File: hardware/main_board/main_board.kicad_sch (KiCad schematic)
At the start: 19 parts, among them IC1 E22-900M22S, IC2 INA226AIDGST, IC3 INA226AIDGST, J3 I2C External Modules, U2 ESP32-C3_SUPERMINI, U3 DS3231SN, U4 FM24CL16B

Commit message: final schema
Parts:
- removed R3: 10k, Resistor_SMD:R_0603_1608Metric, symbol Device:R_Small
- removed U2: ESP32-C3_SUPERMINI, esp32c3_super_mini:MODULE_ESP32-C3_SUPERMINI, symbol ESP32-C3_SUPERMINI:ESP32-C3_SUPERMINI
- added C1, C4: 10uF, Capacitor_SMD:C_0603_1608Metric, symbol Device:C_Small
- added C2: 100nF, Capacitor_SMD:C_0603_1608Metric, symbol Device:C_Small
- added C5, C7: DNP, Capacitor_SMD:C_0603_1608Metric, symbol Device:C_Small
- added C6: 1uF, Capacitor_SMD:C_0603_1608Metric, symbol Device:C_Small
- added J1: EXTERNAL RESET, Connector_JST:JST_EH_B2B-EH-A_1x02_P2.50mm_Vertical, symbol Connector_Generic:Conn_01x02
- added R1, R7: 0R, Resistor_SMD:R_0603_1608Metric, symbol Device:R_Small
- added R10, R12: 10k, Resistor_SMD:R_0603_1608Metric, symbol Device:R_Small
- added R13: 47k, Resistor_SMD:R_0603_1608Metric, symbol Device:R_Small
- added R4: 22R, Resistor_SMD:R_0603_1608Metric, symbol Device:R_Small
- added R8, R9: 4.7k, Resistor_SMD:R_0603_1608Metric, symbol Device:R_Small
- added SW1: RESET, Button_Switch_THT:SW_PUSH_6mm_H5mm, symbol Switch:SW_Push
- added SW2: BOOT, Button_Switch_THT:SW_PUSH_6mm_H5mm, symbol Switch:SW_Push
- added U1: ESP32-C3-WROOM-02, RF_Module:ESP32-C3-WROOM-02, symbol RF_Module:ESP32-C3-WROOM-02
- C10: renamed from C4; Comment (none) -> X7R, ±10%, 16 V
- C11: renamed from C5; Comment (none) -> X7R, ±10%, 16 V
- C3: renamed from C1; Comment (none) -> X7R, ±10%, 16 V
- C8: renamed from C2; Comment (none) -> X7R, ±10%, 16 V
- C9: renamed from C3; Comment (none) -> X7R, ±10%, 16 V
- R11: renamed from R4; Comment (none) -> RF matching element. Populate 0R initially. Value may be ch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
- R5: value 4.7k -> 22R
- R6: value 4.7k -> 470R
- renumbered J3 to J2, R1 to R2, R2 to R3, U3 to U2, U4 to U3
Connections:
- net +3V3: now also J2.2 (Pin_2), C1.1, C2.1, C4.1, R10.1, R12.2, R8.2, R9.2, U1.1 (3V3); no longer J2.1 (Pin_1), R5.2, R6.2
- net CHARGE_SOURCE_STATUS_OUT: now also R12.1, U1.5 (IO6)
- net GND: now also J2.1 (Pin_1), C1.2, C2.2, C4.2, C5.2, C6.2, C7.2, J1.2 (Pin_2), R13.2, SW1.2, SW2.2, U1.19 (GND), U1.9 (GND); no longer J2.2 (Pin_2)
- net I2C_SCL: now also R9.1, U1.7 (IO8); no longer R6.1
- net I2C_SDA: now also R8.1, U1.6 (IO7); no longer R5.1
- net LORA_BUSY: now also U1.18 (IO0)
- net LORA_DIO1: now also U1.11 (IO20/RXD)
- net LORA_NRST: now also SW2.1, U1.8 (IO9)
- net LORA_NSS: now also U1.10 (IO10)
- net SPI_MISO: now also U1.15 (IO3)
- net SPI_MOSI: now also U1.3 (IO4)
- net SPI_SCK: now also U1.4 (IO5)
- net WAKE_IRQ: now also R13.1, U1.17 (IO1)
- net LORA_RXEN: now reaches IC1.6 (RXEN), R2.1
- net LORA_RXEN: now also R1.1
- net at R11.2: now also AE1.1 (A), C7.1; no longer IC1.21 (ANT)
- net LORA_TXEN: now reaches IC1.7 (TXEN), IC1.8 (DIO2)
- net at R11.1: now also C5.1, R7.2; no longer AE1.1 (A)
- new net: R5.1, U1.13 (IO18)
- new net: C6.1, R10.2, R6.1, SW1.1, U1.2 (EN)
- new net: J1.1 (Pin_1), R6.2
- new net: R1.2, U1.12 (IO21/TXD)
- new net: IC1.21 (ANT), R7.1
- new net: R4.2, U1.14 (IO19)
- new net USB_D+: R4.1
- new net USB_D-: R5.2
- no-connect marks 8 -> 6
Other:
- note added: "868 MHz RF MATCHING NETWORK R7/R11 = 0R initially C5/C7 = DNP initially Final values determined by VNA measurement on assembled PCB. If populated, capacitors must be C0G/NP0 RF-grade."
- note added: "Battery current monitor. Shunt = R19 20mR. Firmware calibration must match actual shunt value."
- note added: "INA226: переводити в Power-Down між вимірюваннями"
- note added: "Resistors unless otherwise specified: ±1%, ≥0.1 W, ≤100 ppm/°C. 100 nF / 1 µF MLCC: X7R, ±10%, voltage rating as specified. Bulk MLCC ≥4.7 µF: X5R or X7R, ±20%, verify effective capacitance under DC bias. Do not use Y5V/Z5U capacitors. DNP = Do Not Populate. All components intended for outdoor operation: industrial temperature grade preferred (-40…+85 °C or better)."
- note added: "Solar current monitor. Shunt = R15 100mR. Firmware calibration must match actual shunt value."
- note added: "footprint DS3231M, він сумісний із DS3231SN"
- note added: "max 400 kHz"
- note removed: "INA226AIDGST треба програмно відправляти в deep sleep, щоб він не працював постійно"
- note removed: "Монітор струму та заряду акумулятора"
- note removed: "Скільки W генерує сонячна панель"
- title: (none) -> main
- moved on the sheet: AE1, C10, C3, C8, IC1, J2, R11, R2, R3, U2, U3

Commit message: hw start board
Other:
- moved on the sheet: C6, R10
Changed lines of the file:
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@@
 	)
 	(junction
-		(at 86.36 107.95)
+		(at 88.9 107.95)
 		(diameter 0)
 		(color 0 0 0 0)
@@
 	(wire
 		(pts
-			(xy 86.36 107.95) (xy 86.36 109.22)
+			(xy 88.9 107.95) (xy 88.9 109.22)
 		)
 		(stroke
@@
 	(wire
 		(pts
-			(xy 78.74 107.95) (xy 86.36 107.95)
+			(xy 78.74 107.95) (xy 88.9 107.95)
 		)
 		(stroke
@@
 	(wire
 		(pts
-			(xy 86.36 106.68) (xy 86.36 107.95)
+			(xy 88.9 106.68) (xy 88.9 107.95)
 		)
 		(stroke
@@
 	(symbol
 		(lib_id "power:+3V3")
-		(at 86.36 101.6 0)
+		(at 88.9 101.6 0)
 		(mirror y)
 		(unit 1)
@@
 		(fields_autoplaced yes)
 		(property "Reference" "#PWR015"
-			(at 86.36 105.41 0)
+			(at 88.9 105.41 0)
 			(hide yes)
 			(show_name no)
@@
 		)
 		(property "Value" "+3V3"
-			(at 86.36 96.52 0)
+			(at 88.9 96.52 0)
 			(show_name no)
 			(do_not_autoplace no)
@@
 		)
 		(property "Footprint" ""
-			(at 86.36 101.6 0)
+			(at 88.9 101.6 0)
 			(hide yes)
 			(show_name no)
@@
 		)
 		(property "Datasheet" ""
-			(at 86.36 101.6 0)
+			(at 88.9 101.6 0)
 			(hide yes)
 			(show_name no)
@@
 		)
 		(property "Description" "Power symbol creates a global label with name \"+3V3\""
-			(at 86.36 101.6 0)
+			(at 88.9 101.6 0)
 			(hide yes)
 			(show_name no)
@@
 	(symbol
 		(lib_id "Device:R_Small")
-		(at 86.36 104.14 0)
+		(at 88.9 104.14 0)
 		(mirror y)
 		(unit 1)
@@
 		(dnp no)
 		(property "Reference" "R10"
-			(at 91.44 104.14 90)
+			(at 93.98 104.14 90)
 			(show_name no)
 			(do_not_autoplace no)
@@
 		)
 		(property "Value" "10k"
-			(at 88.9 104.14 90)
+			(at 91.44 104.14 90)
 			(show_name no)
 			(do_not_autoplace no)
@@
 		)
 		(property "Footprint" "Resistor_SMD:R_0603_1608Metric"
-			(at 86.36 104.14 0)
+			(at 88.9 104.14 0)
 			(hide yes)
 			(show_name no)
@@
 		)
 		(property "Datasheet" ""
-			(at 86.36 104.14 0)
+			(at 88.9 104.14 0)
 			(hide yes)
 			(show_name no)
@@
 		)
 		(property "Description" "Resistor, small symbol"
-			(at 86.36 104.14 0)
+			(at 88.9 104.14 0)
 			(hide yes)
 			(show_name no)
@@
 	(symbol
 		(lib_id "power:GND")
-		(at 86.36 114.3 0)
+		(at 88.9 114.3 0)
 		(unit 1)
 		(body_style 1)
@@
 		(fields_autoplaced yes)
 		(property "Reference" "#PWR016"
-			(at 86.36 120.65 0)
+			(at 88.9 120.65 0)
 			(hide yes)
 			(show_name no)
@@
 		)
 		(property "Value" "GND"
-			(at 86.3599 118.11 90)
+			(at 88.8999 118.11 90)
 			(show_name no)
 			(do_not_autoplace no)
@@
 		)
 		(property "Footprint" ""
-			(at 86.36 114.3 0)
+			(at 88.9 114.3 0)
 			(hide yes)
 			(show_name no)
@@
 		)
 		(property "Datasheet" ""
-			(at 86.36 114.3 0)
+			(at 88.9 114.3 0)
 			(hide yes)
 			(show_name no)
@@
 		)
 		(property "Description" "Power symbol creates a global label with name \"GND\" , ground"
-			(at 86.36 114.3 0)
+			(at 88.9 114.3 0)
 			(hide yes)
 			(show_name no)
@@
 	(symbol
 		(lib_id "Device:C_Small")
-		(at 86.36 111.76 0)
+		(at 88.9 111.76 0)
 		(mirror y)
 		(unit 1)
@@
 		(dnp no)
 		(property "Reference" "C6"
-			(at 88.9 113.0365 0)
+			(at 91.44 113.0365 0)
 			(show_name no)
 			(do_not_autoplace no)
@@
 		)
 		(property "Value" "1uF"
-			(at 88.9 110.4965 0)
+			(at 91.44 110.4965 0)
 			(show_name no)
 			(do_not_autoplace no)
@@
 		)
 		(property "Footprint" "Capacitor_SMD:C_0603_1608Metric"
-			(at 86.36 111.76 0)
+			(at 88.9 111.76 0)
 			(hide yes)
 			(show_name no)
@@
 		)
 		(property "Datasheet" ""
-			(at 86.36 111.76 0)
+			(at 88.9 111.76 0)
 			(hide yes)
 			(show_name no)
@@
 		)
 		(property "Description" "Unpolarized capacitor, small symbol"
-			(at 86.36 111.76 0)
+			(at 88.9 111.76 0)
 			(hide yes)
 			(show_name no)
@@
 		)
 		(property "Comment" "X7R, ±10%, ≥10 V"
-			(at 86.36 111.76 0)
+			(at 88.9 111.76 0)
 			(hide yes)
 			(show_name no)

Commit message: hw pcb
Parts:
- added TP10: TP_GND_RF, TestPoint:TestPoint_Pad_D1.0mm, symbol Connector:TestPoint_Small
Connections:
- net GND: now also TP10.1
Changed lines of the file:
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@@
 	)
 	(junction
+		(at 55.88 73.66)
+		(diameter 0)
+		(color 0 0 0 0)
+	)
+	(junction
 		(at 74.93 135.89)
 		(diameter 0)
@@
 	(wire
 		(pts
+			(xy 59.69 73.66) (xy 55.88 73.66)
+		)
+		(stroke
+			(width 0)
+			(type default)
+		)
+	)
+	(wire
+		(pts
 			(xy 55.88 27.94) (xy 55.88 30.48)
 		)
@@
 	(wire
 		(pts
+			(xy 55.88 71.12) (xy 55.88 73.66)
+		)
+		(stroke
+			(width 0)
+			(type default)
+		)
+	)
+	(wire
+		(pts
 			(xy 41.91 53.34) (xy 43.18 53.34)
 		)
@@
 	)
 	(symbol
+		(lib_id "Connector:TestPoint_Small")
+		(at 59.69 73.66 90)
+		(mirror x)
+		(unit 1)
+		(body_style 1)
+		(exclude_from_sim no)
+		(in_bom yes)
+		(on_board yes)
+		(in_pos_files yes)
+		(dnp no)
+		(property "Reference" "TP10"
+			(at 65.532 74.676 90)
+			(show_name no)
+			(do_not_autoplace no)
+			(effects
+				(font
+					(size 1.27 1.27)
+				)
+			)
+		)
+		(property "Value" "TP_GND_RF"
+			(at 65.532 72.136 90)
+			(show_name no)
+			(do_not_autoplace no)
+			(effects
+				(font
+					(size 1.27 1.27)
+				)
+			)
+		)
+		(property "Footprint" "TestPoint:TestPoint_Pad_D1.0mm"
+			(at 59.69 78.74 0)
+			(hide yes)
+			(show_name no)
+			(do_not_autoplace no)
+			(effects
+				(font
+					(size 1.27 1.27)
+				)
+			)
+		)
+		(property "Datasheet" ""
+			(at 59.69 78.74 0)
+			(hide yes)
+			(show_name no)
+			(do_not_autoplace no)
+			(effects
+				(font
+					(size 1.27 1.27)
+				)
+			)
+		)
+		(property "Description" "test point"
+			(at 59.69 73.66 0)
+			(hide yes)
+			(show_name no)
+			(do_not_autoplace no)
+			(effects
+				(font
+					(size 1.27 1.27)
+				)
+			)
+		)
+		(pin "1"
+		)
+		(instances
+			(project "main_board"
+				(path "/c188e145-349d-484e-a5ed-94efd42d01f5"
+					(reference "TP10")
+					(unit 1)
+				)
+			)
+		)
+	)
+	(symbol
 		(lib_id "power:GND")
 		(at 236.22 87.63 270)
@@
 	(symbol
 		(lib_id "power:GND")
-		(at 55.88 71.12 0)
+		(at 55.88 73.66 0)
 		(mirror y)
 		(unit 1)
@@
 		(dnp no)
 		(property "Reference" "#PWR010"
-			(at 55.88 77.47 0)
+			(at 55.88 80.01 0)
 			(hide yes)
 			(show_name no)
@@
 		)
 		(property "Value" "GND"
-			(at 55.8799 74.93 90)
+			(at 55.8799 77.47 90)
 			(show_name no)
 			(do_not_autoplace no)
@@
 		)
 		(property "Footprint" ""
-			(at 55.88 71.12 0)
+			(at 55.88 73.66 0)
 			(hide yes)
 			(show_name no)
@@
 		)
 		(property "Datasheet" ""
-			(at 55.88 71.12 0)
+			(at 55.88 73.66 0)
 			(hide yes)
 			(show_name no)
@@
 		)
 		(property "Description" "Power symbol creates a global label with name \"GND\" , ground"
-			(at 55.88 71.12 0)
+			(at 55.88 73.66 0)
 			(hide yes)
 			(show_name no)
@@
 			"0422116d-5074-45fc-80d8-820c768ad917" "083d04f3-e587-461c-8ba0-c13e53402020"
 			"113aeb92-e46f-40ed-bd7d-62368046a4bd" "134f9fee-9054-457e-9bb8-6b6e1295af7a"
-			"16155f65-256a-4ea7-bec3-5b9b045cd330" "19ab73e4-bc5b-4864-ac6d-62388520e02c"
-			"1bbc02cd-1e9b-4023-b0a0-1f2260bc69ab" "1e106cdd-49bc-4cc3-ba8c-91a0c60a2d9e"
-			"275a0193-e6fa-487d-a717-21a96c1f61ba" "297f4761-4462-4170-87bb-e8c8ef9e76a1"
-			"2e4da865-29f6-4bd1-b4cf-b40c526e7e11" "2f756d60-1b35-4199-bb02-bcadc4bb8d59"
-			"307f79be-0e2a-49ad-9417-b6a072f862d8" "37c88614-624c-4cbc-a9ba-b282e3c5f7b2"
-			"3a119ae1-638f-4c5d-bec3-c70eb130e683" "3f8adb90-bcd0-470c-a794-7af98dd90b83"
-			"41bc5960-3101-4704-9075-af10071a797c" "49194eb5-692b-4ba1-8ef2-f23034a67c94"
-			"4d6e359a-efac-481e-bf7e-0d8f49461477" "4f6617a8-875a-46ce-835c-d3e49d7aabe5"
-			"5bbc5b9f-0ba1-47ec-8af7-acfb001eb1d4" "63462031-cd51-4a31-a75f-030f5d628ae4"
+			"16155f65-256a-4ea7-bec3-5b9b045cd330" "16bf33e3-a02c-4b6b-b4b0-71e6f3a21441"
+			"19ab73e4-bc5b-4864-ac6d-62388520e02c" "1bbc02cd-1e9b-4023-b0a0-1f2260bc69ab"
+			"1e106cdd-49bc-4cc3-ba8c-91a0c60a2d9e" "275a0193-e6fa-487d-a717-21a96c1f61ba"
+			"297f4761-4462-4170-87bb-e8c8ef9e76a1" "2e4da865-29f6-4bd1-b4cf-b40c526e7e11"
+			"2f756d60-1b35-4199-bb02-bcadc4bb8d59" "307f79be-0e2a-49ad-9417-b6a072f862d8"
+			"37c88614-624c-4cbc-a9ba-b282e3c5f7b2" "3a119ae1-638f-4c5d-bec3-c70eb130e683"
+			"3f8adb90-bcd0-470c-a794-7af98dd90b83" "41bc5960-3101-4704-9075-af10071a797c"
+			"49194eb5-692b-4ba1-8ef2-f23034a67c94" "4d6e359a-efac-481e-bf7e-0d8f49461477"
+			"4f6617a8-875a-46ce-835c-d3e49d7aabe5" "5bbc5b9f-0ba1-47ec-8af7-acfb001eb1d4"
+			"62032db8-9efe-466c-bb62-8552b6f2bde3" "63462031-cd51-4a31-a75f-030f5d628ae4"
 			"63821ea0-9264-4ab2-a0e7-35959071552e" "6781b633-a1e5-4a82-aeff-2637d55213fa"
 			"681d5124-6748-4ced-8ab4-53ca74655802" "6bf3a4d0-9919-450c-8e28-8261ae80585a"
@@
 			"8302702b-c6f7-4432-914c-84afed3b04cb" "84ce62cf-80e1-4a02-a711-e17b2517579a"
 			"87c8591a-2414-413a-892d-de1b675c2120" "88e5e9c2-fbb9-42ba-bf50-35309971f1b2"
-			"8de96f5e-7a5f-433d-8d27-861beaf929ea" "9b5263d4-47c8-4543-8404-aeb70e442a5e"
-			"a30ebfd5-8556-420e-a85b-9e41fd03a8dd" "a454f0c8-0178-4877-89f9-d8804a7784ae"
-			"ae02fce1-5d38-4ffd-8a8c-448e73865403" "aeb43d10-145f-4ba8-9ded-732c7d0fbe7e"
-			"af2c52f1-c2a7-4d0d-aca3-4484cc8ad686" "b1705b6d-3e2f-4144-abe5-5c96bf92c17c"
+			"8911399a-8c94-4901-819a-c51443d45adc" "8de96f5e-7a5f-433d-8d27-861beaf929ea"
+			"9b5263d4-47c8-4543-8404-aeb70e442a5e" "a30ebfd5-8556-420e-a85b-9e41fd03a8dd"
+			"a454f0c8-0178-4877-89f9-d8804a7784ae" "ae02fce1-5d38-4ffd-8a8c-448e73865403"
+			"aeb43d10-145f-4ba8-9ded-732c7d0fbe7e" "af2c52f1-c2a7-4d0d-aca3-4484cc8ad686"
+			"b1705b6d-3e2f-4144-abe5-5c96bf92c17c" "b67e7214-1fc0-4129-8fb6-fc7df31daa2c"
 			"b763b5e5-ebca-4580-8da7-27c65c442b92" "b86c327f-a85d-4d1a-8e2d-fbfa0cc3c3e2"
 			"b8f4bbdd-a851-4aa2-a24f-dc8ff6999511" "bafe1022-fb04-4374-b31e-a1180c9b7ebc"

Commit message: hw pcb v0.2
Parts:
- removed J1: EXTERNAL RESET, Connector_JST:JST_EH_B2B-EH-A_1x02_P2.50mm_Vertical, symbol Connector_Generic:Conn_01x02
- removed R6: 470R, Resistor_SMD:R_0603_1608Metric, symbol Device:R_Small
- removed SW1: RESET, Button_Switch_THT:SW_PUSH_6mm_H5mm, symbol Switch:SW_Push
- removed SW2: BOOT, Button_Switch_THT:SW_PUSH_6mm_H5mm, symbol Switch:SW_Push
- added TP6: ESP32_EN, TestPoint:TestPoint_Pad_D1.5mm, symbol Connector:TestPoint_Small
- TP10: value TP_GND_RF -> ESP32_BOOT; footprint TestPoint:TestPoint_Pad_D1.0mm -> TestPoint:TestPoint_Pad_D1.5mm
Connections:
- net GND: no longer TP10.1
- net LORA_NRST: now also TP10.1
- net at C6.1, R10.2, U1.2 (EN): now also TP6.1
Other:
- note added: "NOT FOR V1"
- moved on the sheet: C6, R10

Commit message: hw v1 add PCA9536DR
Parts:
- added C24: 100nF, Capacitor_SMD:C_0603_1608Metric, symbol Device:C_Small
- added U5: PCA9536DR, Package_SO:SOIC-8_3.9x4.9mm_P1.27mm, symbol Interface_Expansion:PCA9536D
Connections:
- net +3V3: now also C24.1, U5.8 (VDD); no longer IC3.2 (A0)
- net GND: now also IC3.2 (A0), C24.2, U5.4 (VSS)
- net I2C_SCL: now also U5.6 (SCL)
- net I2C_SDA: now also U5.7 (SDA)
- new net CHRG_STATUS: U5.1 (IO0)
- new net STDBY_STATUS: U5.2 (IO1)
- no-connect marks 6 -> 8
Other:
- note added: "address: 0x40"
- moved on the sheet: C10, C8, J2, R13, U2, U3

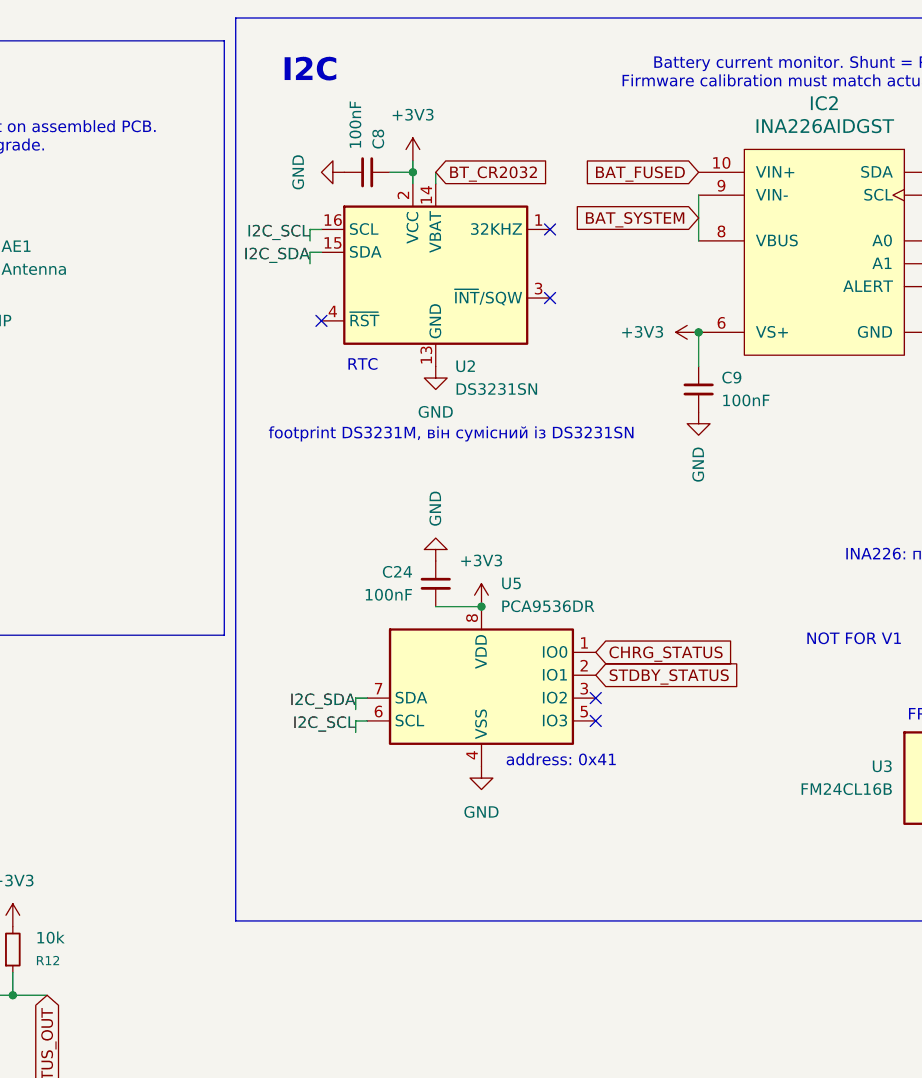
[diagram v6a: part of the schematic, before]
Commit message: hw v1 wi-fi switch
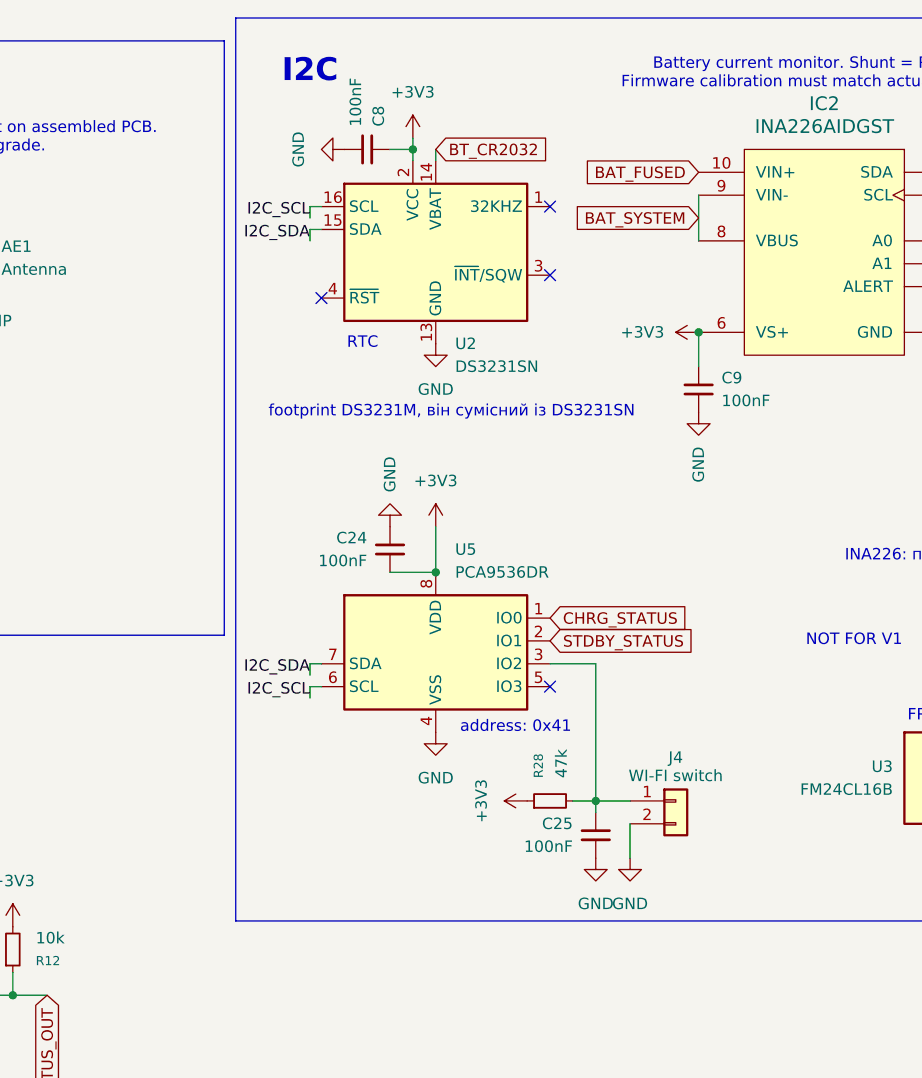
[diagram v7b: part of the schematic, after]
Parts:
- added C25: 100nF, Capacitor_SMD:C_0603_1608Metric, symbol Device:C_Small
- added J4: WI-FI switch, Connector_JST:JST_PH_B2B-PH-K_1x02_P2.00mm_Vertical, symbol Connector_Generic:Conn_01x02
- added R28: 47k, Resistor_SMD:R_0603_1608Metric, symbol Device:R_Small
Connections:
- net +3V3: now also R28.1
- net GND: now also C25.1, J4.2 (Pin_2)
- net at U5.3 (IO2): now also C25.2, J4.1 (Pin_1), R28.2
- no-connect marks 8 -> 7
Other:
- moved on the sheet: C24, C8, U2, U5
